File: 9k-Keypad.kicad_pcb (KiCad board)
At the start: 2 copper layers, 61.9 x 86.5 mm, 34 parts, among them SW1 SW_Push, U1 ATmega32U4-AU, Y1 16MHz

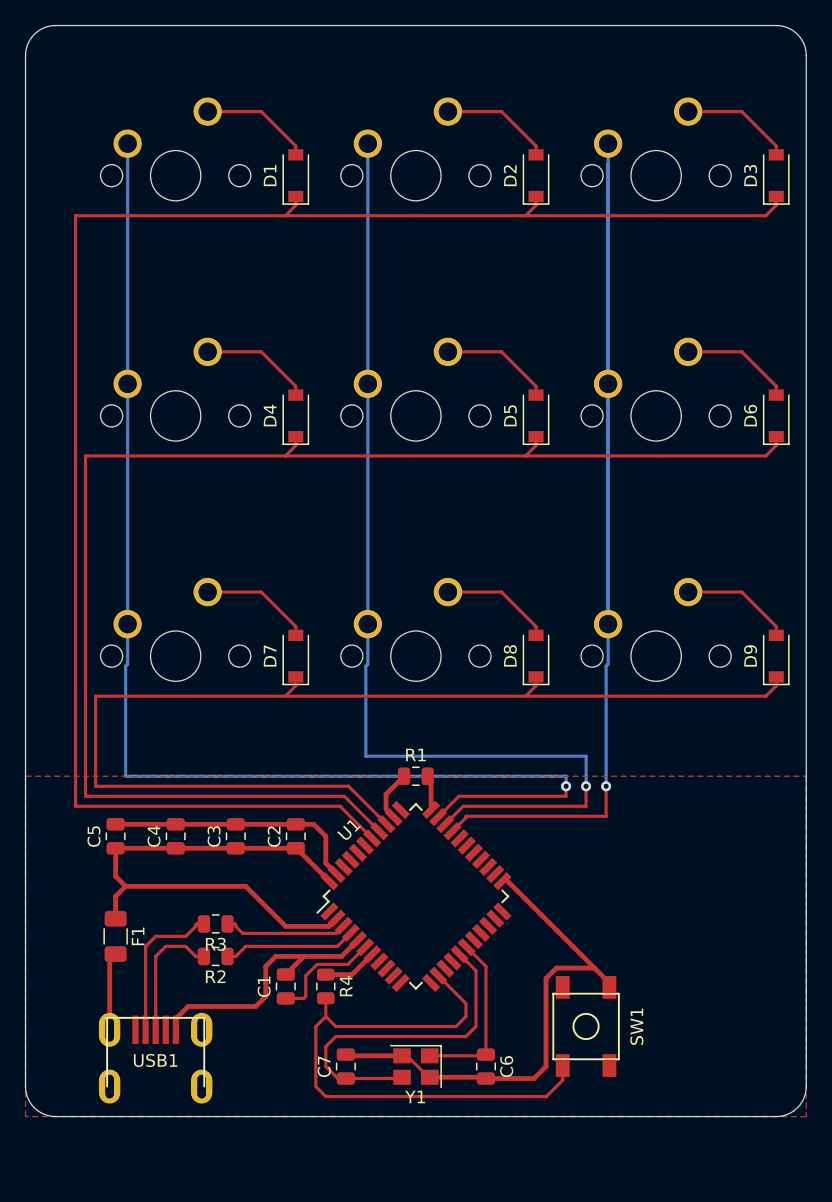
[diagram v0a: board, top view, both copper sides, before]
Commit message: new layout and USB-C
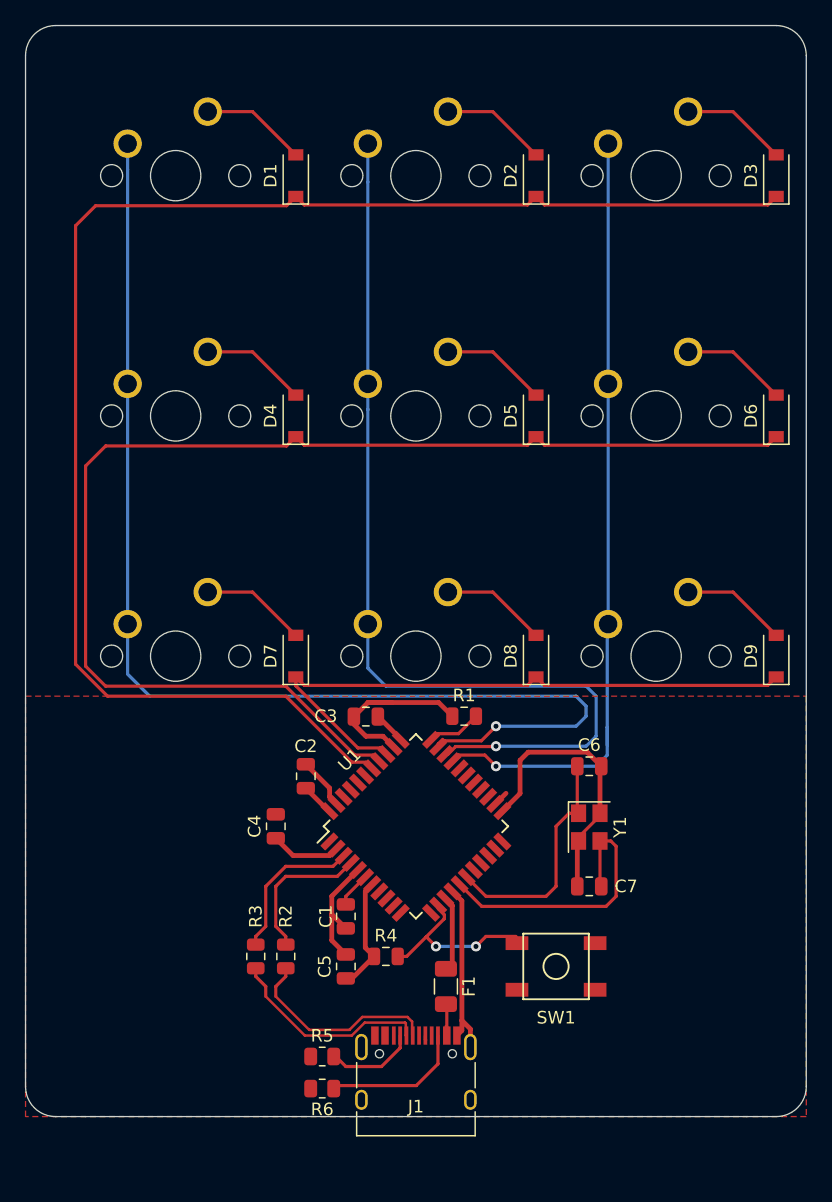
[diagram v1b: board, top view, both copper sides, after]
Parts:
- removed USB1: Molex-0548190589, random-keyboard-parts:Molex-0548190589
- added J1: USB_C_Receptacle_USB2.0, Connector_USB:USB_C_Receptacle_HRO_TYPE-C-31-M-12, F.Cu at (74.6, 126.2)
- added R5: 5k1, Resistor_SMD:R_0805_2012Metric, F.Cu at (67.2, 123.8)
- added R6: 5k1, Resistor_SMD:R_0805_2012Metric, F.Cu at (67.2, 126.4)
- moved F1 26.5 mm to (77.0, 118.3)
- moved C6 25.2 mm to (88.4, 100.8), turned to 0 degrees
- moved C7 24.0 mm to (88.4, 110.3), turned to 180 degrees
- moved Y1 23.4 mm to (88.4, 105.6), turned to 270 degrees
- moved C5 21.0 mm to (69.1, 116.7)
- moved C3 14.0 mm to (70.6, 96.9), turned to 180 degrees
- moved C4 7.98 mm to (63.5, 105.6)
- moved C1 7.32 mm to (69.1, 112.7), turned to 270 degrees
- moved R1 6.11 mm to (78.4, 96.8)
- moved R2 5.56 mm to (64.3, 115.9), turned to 270 degrees
- moved U1 5.56 mm to (74.6, 105.6)
- moved R4 5.32 mm to (72.2, 115.9), turned to 0 degrees
- moved SW1 5.32 mm to (85.7, 116.7), turned to 0 degrees
- moved C2 4.83 mm to (65.9, 101.6)
- moved R3 4.09 mm to (61.9, 115.9), turned to 270 degrees
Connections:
- U1 pad 1: Net-(U1-Pad1) -> (no net)
- U1 pad 10: Net-(U1-Pad10) -> (no net)
- U1 pad 11: Net-(U1-Pad11) -> (no net)
- U1 pad 12: Net-(U1-Pad12) -> (no net)
- U1 pad 18: Net-(U1-Pad18) -> (no net)
- U1 pad 19: Net-(U1-Pad19) -> (no net)
- U1 pad 20: Net-(U1-Pad20) -> (no net)
- U1 pad 21: Net-(U1-Pad21) -> (no net)
- U1 pad 22: Net-(U1-Pad22) -> (no net)
- U1 pad 25: Net-(U1-Pad25) -> (no net)
- U1 pad 26: Net-(U1-Pad26) -> (no net)
- U1 pad 27: Net-(U1-Pad27) -> (no net)
- U1 pad 28: Net-(U1-Pad28) -> (no net)
- U1 pad 29: Net-(U1-Pad29) -> (no net)
- U1 pad 39: Net-(U1-Pad39) -> (no net)
- U1 pad 40: Net-(U1-Pad40) -> (no net)
- U1 pad 41: Net-(U1-Pad41) -> (no net)
- U1 pad 42: Net-(U1-Pad42) -> (no net)
- U1 pad 8: Net-(U1-Pad8) -> (no net)
- U1 pad 9: Net-(U1-Pad9) -> (no net)
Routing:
- net ROW2: track 90.2 -> 49.3 mm
- net COL2: track 104.0 -> 63.1 mm
- net Net-(R4-Pad2): track 44.8 -> 13.9 mm, vias 0 -> 2
- net GND: track 86.4 -> 65.3 mm
- net +5V: track 46.9 -> 27.8 mm
- net ROW0: track 131.7 -> 119.4 mm
- net ROW1: track 111.0 -> 99.1 mm
- net Net-(J1-PadB5): track 0.00 -> 11.3 mm
- net Net-(J1-PadA5): track 0.00 -> 7.19 mm
- net D+: track 10.3 -> 16.5 mm
- net Net-(C1-Pad1): track 8.94 -> 2.80 mm
- net COL1: track 81.8 -> 76.3 mm
- net Net-(C7-Pad1): track 27.8 -> 22.5 mm
- net Net-(C6-Pad1): track 13.6 -> 18.8 mm
- net D-: track 12.0 -> 17.0 mm
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
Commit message: compacted layouyt
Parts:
- added REF**: MountingHole_3.5mm, MountingHole:MountingHole_3.5mm, F.Cu at (47.6, 129.4)
- added REF**: MountingHole_3.5mm, MountingHole:MountingHole_3.5mm, F.Cu at (47.6, 46.0)
- added REF**: MountingHole_3.5mm, MountingHole:MountingHole_3.5mm, F.Cu at (101.6, 46.0)
- added REF**: MountingHole_3.5mm, MountingHole:MountingHole_3.5mm, F.Cu at (101.6, 129.4)
- moved C5 16.3 mm to (83.3, 108.7), turned to 315 degrees
- moved R6 9.92 mm to (76.2, 122.2), turned to 90 degrees
- moved F1 8.55 mm to (69.1, 121.4)
- moved C4 7.32 mm to (65.1, 112.7), turned to 135 degrees
- moved R4 6.78 mm to (78.6, 118.3), turned to 225 degrees
- moved R5 6.05 mm to (73.0, 122.2), turned to 270 degrees
- moved C1 6.05 mm to (66.7, 118.3), turned to 90 degrees
- moved C7 5.56 mm to (88.4, 115.9)
- moved U1 5.56 mm to (74.6, 111.1)
- moved Y1 5.56 mm to (88.4, 111.2)
- moved C6 5.56 mm to (88.4, 106.4)
- moved R1 5.56 mm to (78.4, 102.4), turned to 180 degrees
- moved R2 5.56 mm to (64.3, 121.4)
- moved R3 5.56 mm to (61.9, 121.4)
- moved SW1 5.56 mm to (85.7, 122.2)
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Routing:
- net GND: track 65.3 -> 21.1 mm
- net VCC: track 3.27 -> 17.6 mm, vias 0 -> 3
- net ROW0: track 119.4 -> 133.0 mm
- net ROW1: track 99.1 -> 112.5 mm
- net D-: track 17.0 -> 30.2 mm
- net D+: track 16.5 -> 26.0 mm, vias 0 -> 3
- net Net-(J1-PadB5): track 11.3 -> 2.25 mm
- net COL1: track 76.3 -> 67.6 mm
- net COL0: track 93.8 -> 85.5 mm
- net ROW2: track 49.3 -> 56.8 mm
- net Net-(C7-Pad1): track 22.5 -> 15.8 mm
- net +5V: track 27.8 -> 21.3 mm
- net Net-(R4-Pad2): track 13.9 -> 7.47 mm, vias 2 -> 0
- net Net-(J1-PadA5): track 7.19 -> 2.33 mm
- net Net-(C1-Pad1): track 2.80 -> 5.68 mm
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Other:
- board size 61.9 x 86.5 mm -> 61.9 x 91.3 mm
